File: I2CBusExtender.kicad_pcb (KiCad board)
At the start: 2 copper layers, 57.5 x 17.9 mm, 19 parts, among them J1 SBusConn, J2 LBusCon, U1 P82B715

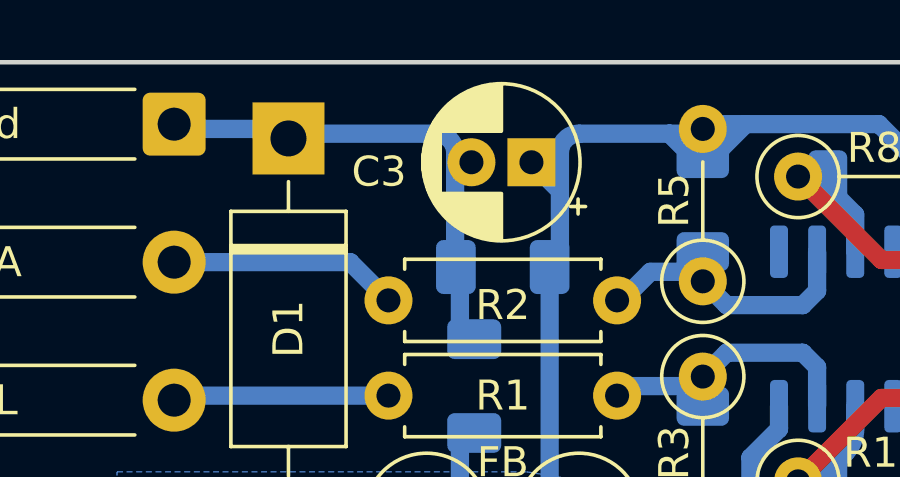
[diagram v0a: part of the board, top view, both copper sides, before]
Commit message: Added teardrops to board front GND plane.
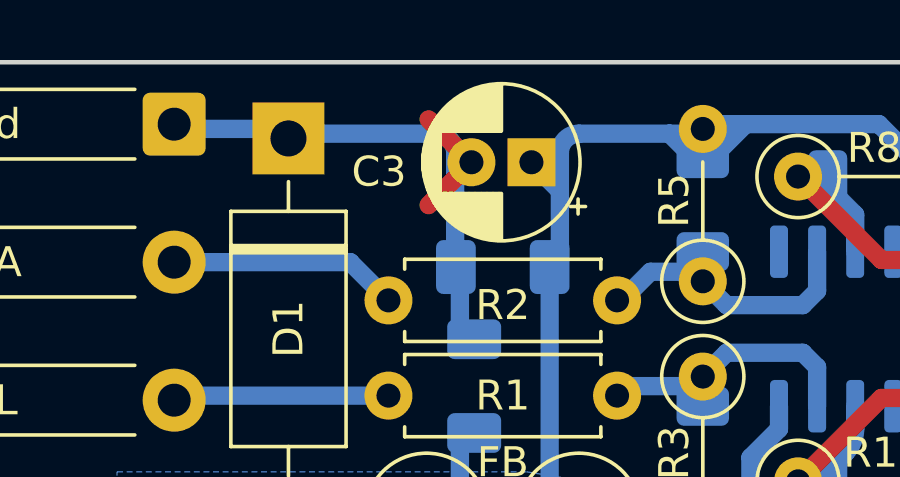
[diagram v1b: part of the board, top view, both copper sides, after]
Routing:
- net /Gnd: track 20.4 -> 24.4 mm
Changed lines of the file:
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@@
   (segment (start 89.205 94.4325) (end 87.9475 93.175) (width 0.6096) (layer "B.Cu") (net 3))
   (segment (start 91.7575 92.55125) (end 91.7575 94.4325) (width 0.6096) (layer "B.Cu") (net 3))
+  (segment (start 97.856363 80.645) (end 96.427613 82.07375) (width 0.6096) (layer "F.Cu") (net 4))
+  (segment (start 97.856363 80.645) (end 96.427613 79.21625) (width 0.6096) (layer "F.Cu") (net 4))
   (via (at 108.10875 93.18625) (size 1.28) (drill 0.7) (layers "F.Cu" "B.Cu") (net 4))
   (segment (start 97.31375 80.645) (end 97.31375 84.1125) (width 0.6096) (layer "B.Cu") (net 4))
